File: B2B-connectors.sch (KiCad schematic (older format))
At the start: 2 parts, among them J3 DF40C-100DP-0.4V(51), J4 DF40C-100DP-0.4V(51)

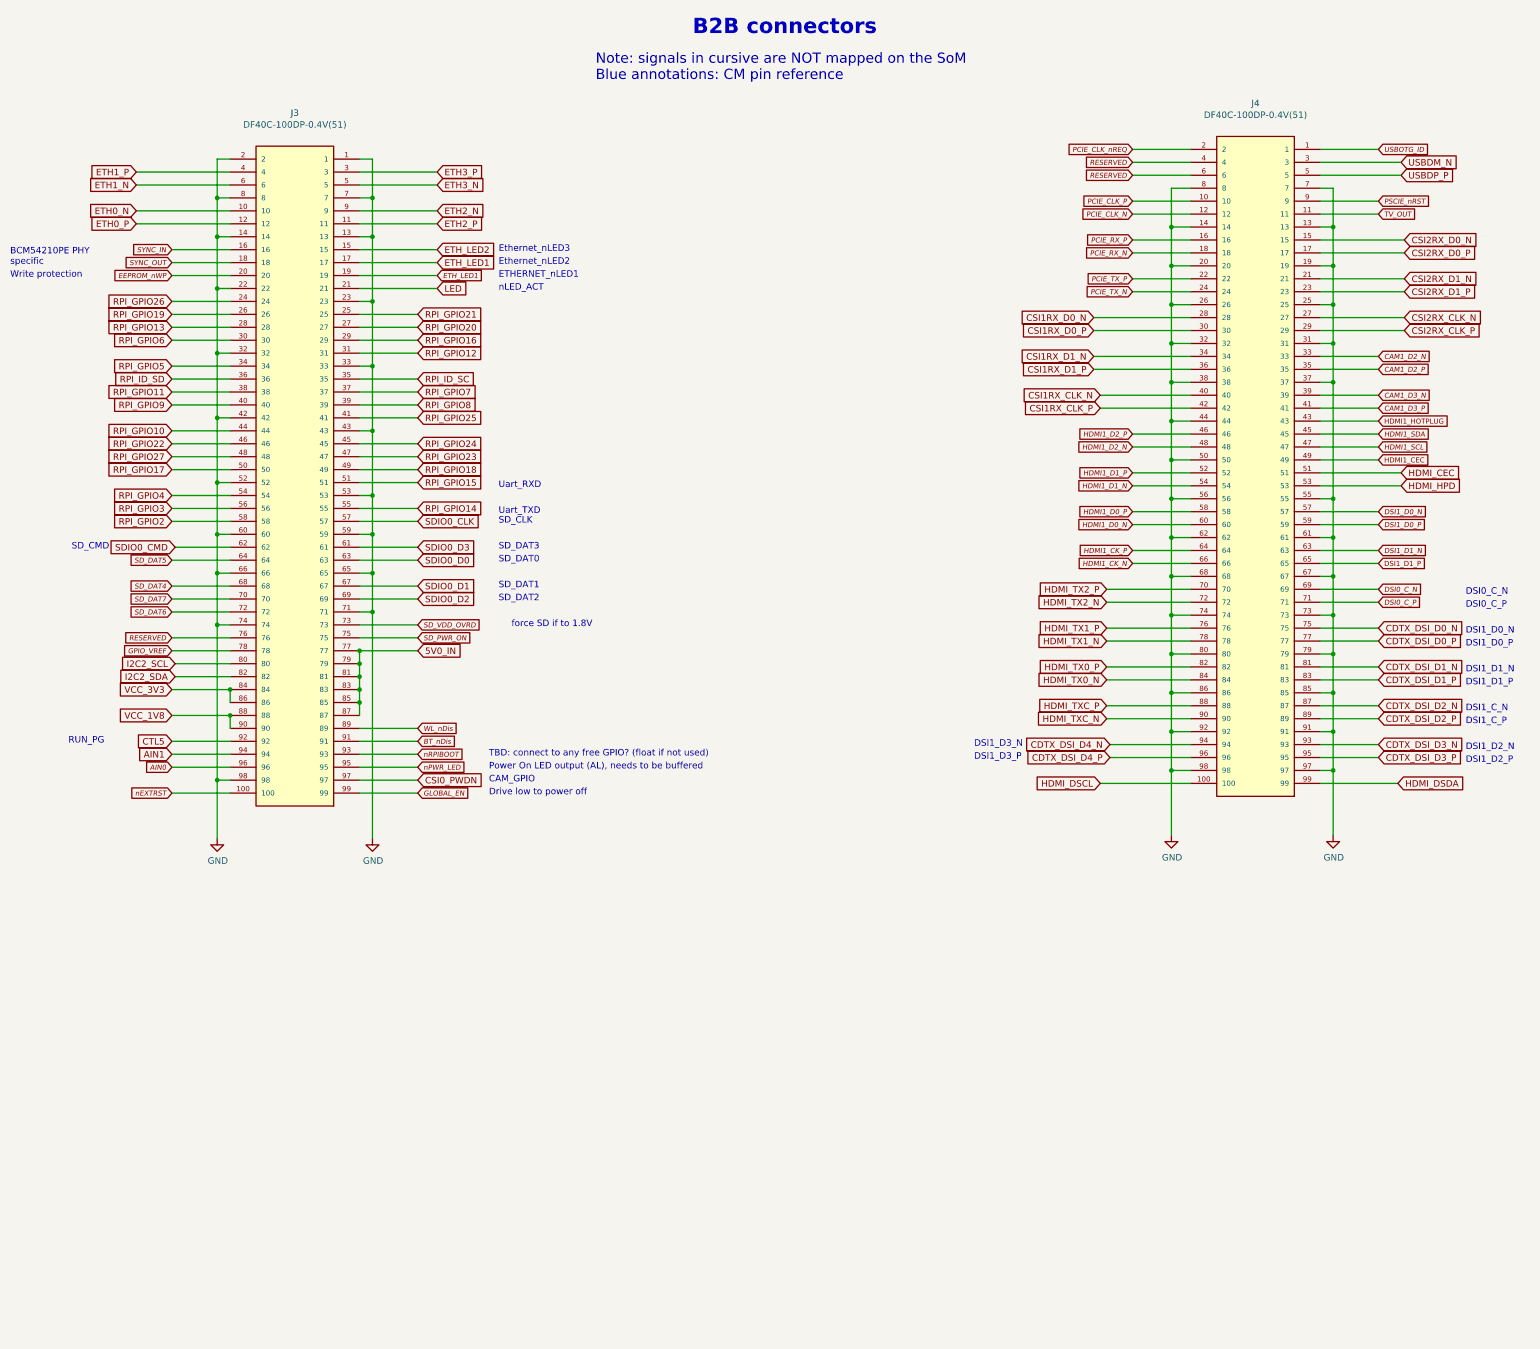
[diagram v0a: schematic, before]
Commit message: Updated GPIO pinout to BV0.9. Remapped DSI. Mapped USB3.0
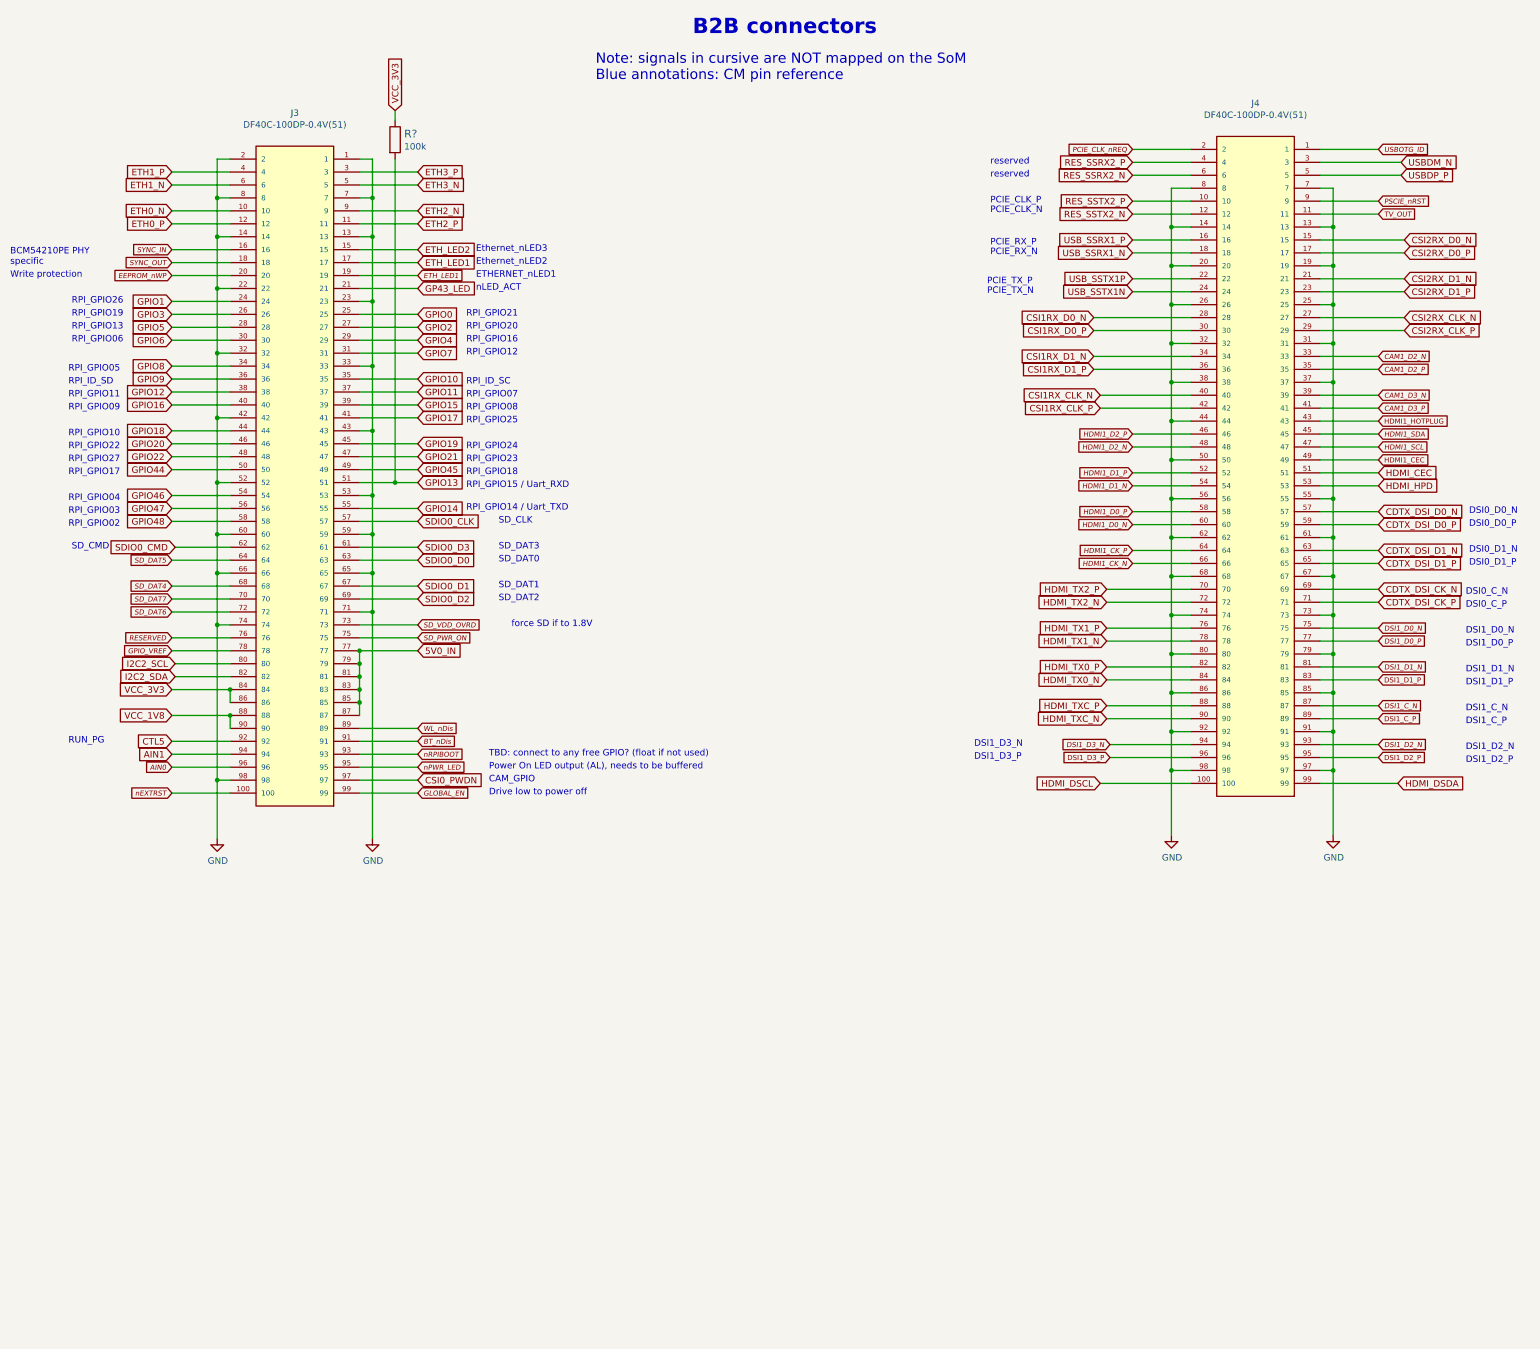
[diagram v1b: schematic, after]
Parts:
- added R?: R_100k_0402, arvsom-footprints:0402-res, symbol arvsom:R_100k_0402
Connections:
- net CDTX_DSI_D0_N: now also J4.57; no longer J4.75
- net CDTX_DSI_D0_P: now also J4.59; no longer J4.77
- net CDTX_DSI_D1_N: now also J4.63; no longer J4.81
- net CDTX_DSI_D1_P: now also J4.65; no longer J4.83
- net DSI1_D0_N: now also J4.75; no longer J4.57
- net DSI1_D0_P: now also J4.77; no longer J4.59
- net DSI1_D1_N: now also J4.81; no longer J4.63
- net DSI1_D1_P: now also J4.83; no longer J4.65
- net RESERVED: no longer J4.4, J4.6
- net VCC_3V3: now also R?.1
- net CDTX_DSI_D2_N renamed DSI1_C_N
- net CDTX_DSI_D2_P renamed DSI1_C_P
- net CDTX_DSI_D3_N renamed DSI1_D2_N
- net CDTX_DSI_D3_P renamed DSI1_D2_P
- net CDTX_DSI_D4_N renamed DSI1_D3_N
- net CDTX_DSI_D4_P renamed DSI1_D3_P
- net DSI0_C_N renamed CDTX_DSI_CK_N
- net DSI0_C_P renamed CDTX_DSI_CK_P
- net LED renamed GP43_LED
- net PCIE_CLK_N renamed RES_SSTX2_N
- net PCIE_CLK_P renamed RES_SSTX2_P
- net PCIE_RX_N renamed USB_SSRX1_N
- net PCIE_RX_P renamed USB_SSRX1_P
- net PCIE_TX_N renamed USB_SSTX1N
- net PCIE_TX_P renamed USB_SSTX1P
- net RPI_GPIO10 renamed GPIO18
- net RPI_GPIO11 renamed GPIO12
- net RPI_GPIO12 renamed GPIO7
- net RPI_GPIO13 renamed GPIO5
- net RPI_GPIO14 renamed GPIO14
- net RPI_GPIO15 renamed GPIO13
- net GPIO13: now also R?.2
- net RPI_GPIO16 renamed GPIO4
- net RPI_GPIO17 renamed GPIO44
- net RPI_GPIO18 renamed GPIO45
- net RPI_GPIO19 renamed GPIO3
- net RPI_GPIO2 renamed GPIO48
- net RPI_GPIO20 renamed GPIO2
- net RPI_GPIO21 renamed GPIO0
- net RPI_GPIO22 renamed GPIO20
- net RPI_GPIO23 renamed GPIO21
- net RPI_GPIO24 renamed GPIO19
- net RPI_GPIO25 renamed GPIO17
- net RPI_GPIO26 renamed GPIO1
- net RPI_GPIO27 renamed GPIO22
- net RPI_GPIO3 renamed GPIO47
- net RPI_GPIO4 renamed GPIO46
- net RPI_GPIO5 renamed GPIO8
- net RPI_GPIO6 renamed GPIO6
- net RPI_GPIO7 renamed GPIO11
- net RPI_GPIO8 renamed GPIO15
- net RPI_GPIO9 renamed GPIO16
- net RPI_ID_SC renamed GPIO10
- net RPI_ID_SD renamed GPIO9
- new net RES_SSRX2_N: J4.6
- new net RES_SSRX2_P: J4.4
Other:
- note added: "DSI0_D0_N"
- note added: "DSI0_D0_P"
- note added: "DSI0_D1_N"
- note added: "DSI0_D1_P"
- note added: "PCIE_CLK_N"
- note added: "PCIE_CLK_P"
- note added: "PCIE_RX_N"
- note added: "PCIE_RX_P"
- note added: "PCIE_TX_N"
- note added: "PCIE_TX_P"
- note added: "RPI_GPIO02"
- note added: "RPI_GPIO03"
- note added: "RPI_GPIO04"
- note added: "RPI_GPIO05"
- note added: "RPI_GPIO06"
- note added: "RPI_GPIO07"
- note added: "RPI_GPIO08"
- note added: "RPI_GPIO09"
- note added: "RPI_GPIO10"
- note added: "RPI_GPIO11"
- note added: "RPI_GPIO12"
- note added: "RPI_GPIO13"
- note added: "RPI_GPIO14 / Uart_TXD"
- note added: "RPI_GPIO15 / Uart_RXD"
- note added: "RPI_GPIO16"
- note added: "RPI_GPIO17"
- note added: "RPI_GPIO18"
- note added: "RPI_GPIO19"
- note added: "RPI_GPIO20"
- note added: "RPI_GPIO21"
- note added: "RPI_GPIO22"
- note added: "RPI_GPIO23"
- note added: "RPI_GPIO24"
- note added: "RPI_GPIO25"
- note added: "RPI_GPIO26"
- note added: "RPI_GPIO27"
- note added: "RPI_ID_SC"
- note added: "RPI_ID_SD"
- note added: "reserved"
- note added: "reserved\n"
- note removed: "Uart_RXD"
- note removed: "Uart_TXD"

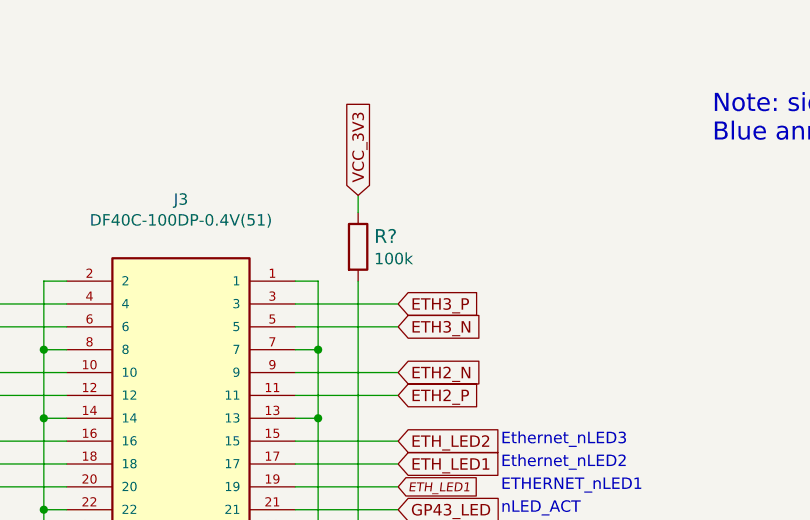
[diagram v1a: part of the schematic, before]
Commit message: Updated VIC config, added reset and crystals
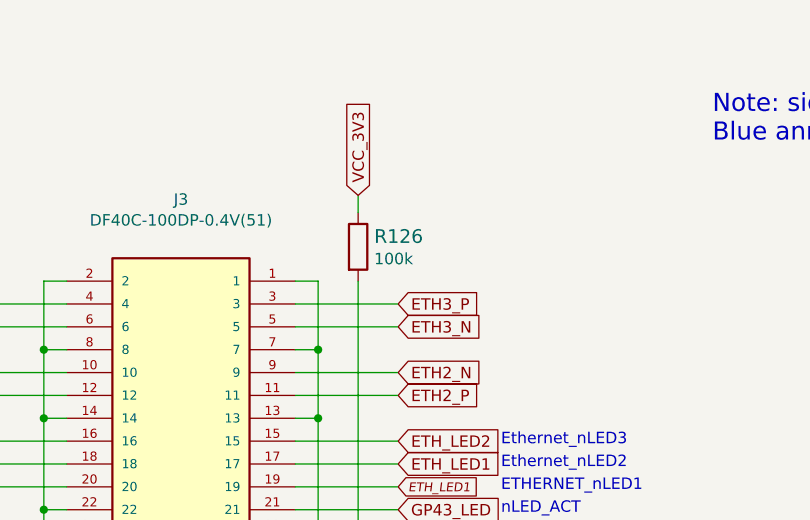
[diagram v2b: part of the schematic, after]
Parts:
- gave numbers to parts that had none: 1
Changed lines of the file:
@@
 	5075 4900 4800 4900
 $Comp
-L arvsom:R_100k_0402 R?
+L arvsom:R_100k_0402 R126
 U 1 1 60AFC161
 P 5075 2250
-F 0 "R?" V 5030 2320 60  0000 L CNN
+F 0 "R126" V 5030 2320 60  0000 L CNN
 F 1 "R_100k_0402" H 5075 2100 60  0001 C CNN
 F 2 "arvsom-footprints:0402-res" H 5275 2450 60  0001 L CNN

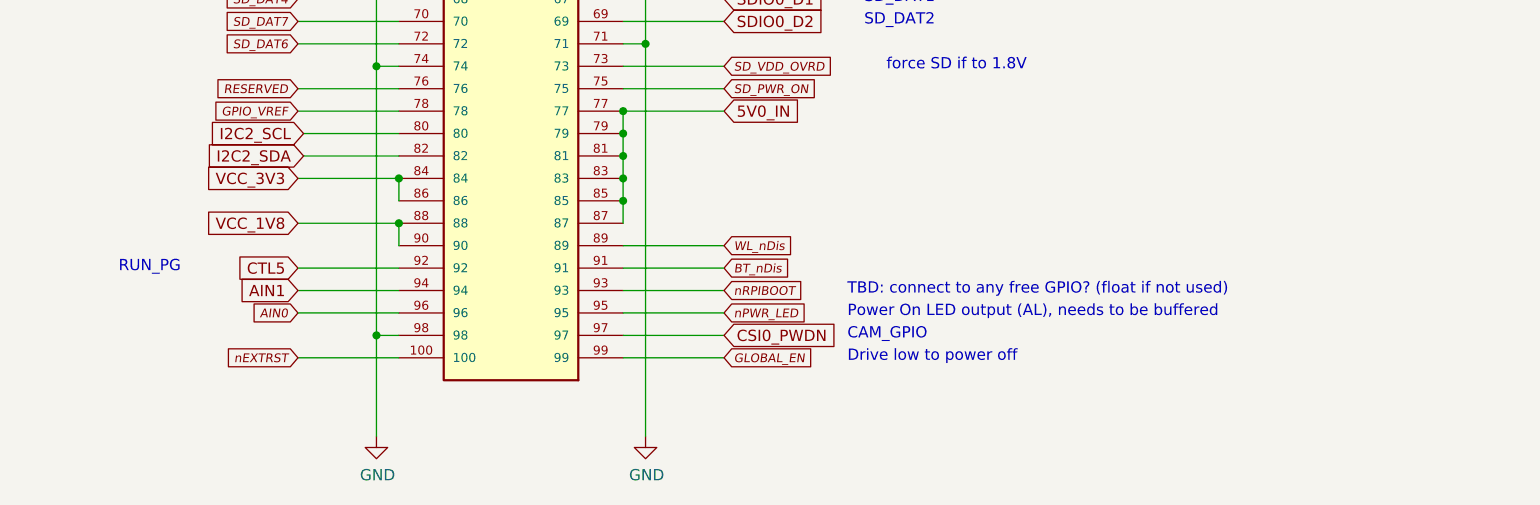
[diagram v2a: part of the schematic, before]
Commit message: Added BOOT_FROM_UART and power LED. Changed LED transistor to smaller footprint
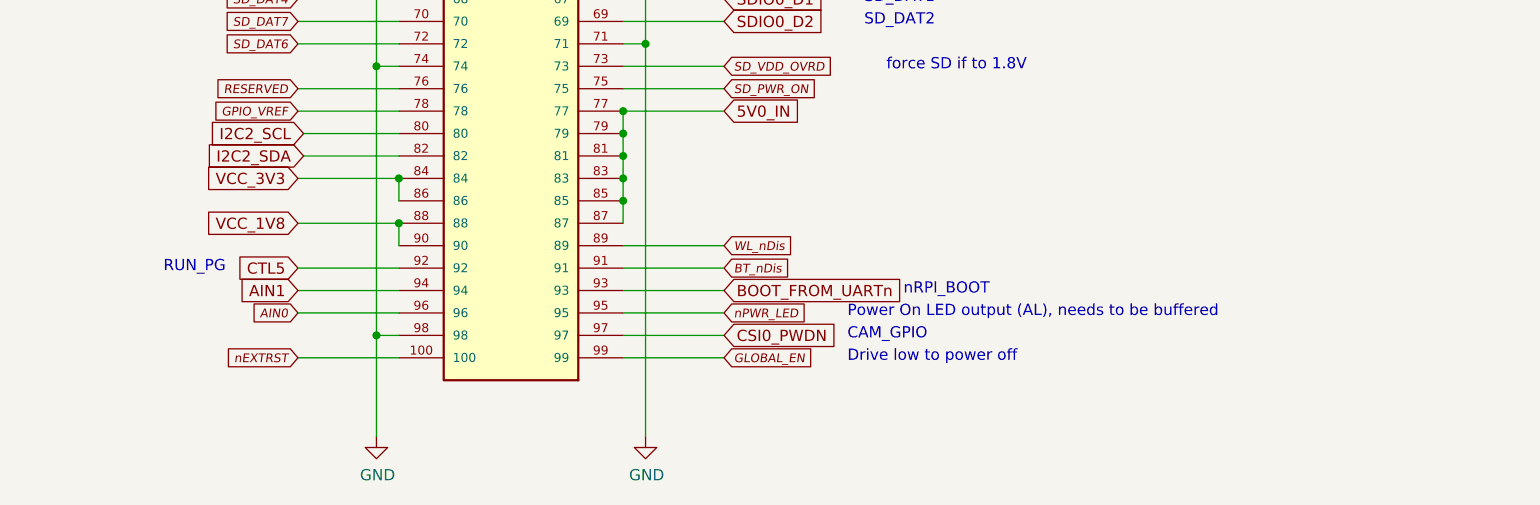
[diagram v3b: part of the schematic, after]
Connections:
- net nRPIBOOT renamed BOOT_FROM_UARTn
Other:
- note added: "nRPI_BOOT"
- note removed: "TBD: connect to any free GPIO? (float if not used)"
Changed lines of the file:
@@
 Wire Wire Line
 	4800 7000 5250 7000
-Text GLabel 5250 7000 2    39   Input Italic 0
-nRPIBOOT
 Wire Wire Line
 	11225 2425 10775 2425
@@
 Text Notes 5800 7225 0    50   ~ 0
 CAM_GPIO
-Text Notes 5800 7025 0    50   ~ 0
-TBD: connect to any free GPIO? (float if not used)
+Text Notes 6050 7025 0    50   ~ 0
+nRPI_BOOT
 Text Notes 5800 7125 0    50   ~ 0
 Power On LED output (AL), needs to be buffered
 Text Notes 5800 7325 0    50   ~ 0
 Drive low to power off
-Text Notes 2550 6925 0    50   ~ 0
+Text Notes 2750 6925 0    50   ~ 0
 RUN_PG
 Text Notes 13350 5775 0    50   ~ 0
@@
 Text Notes 9650 3450 0    50   ~ 0
 PCIE_TX_N
+Text GLabel 5250 7000 2    50   Input ~ 0
+BOOT_FROM_UARTn
 $EndSCHEMATC

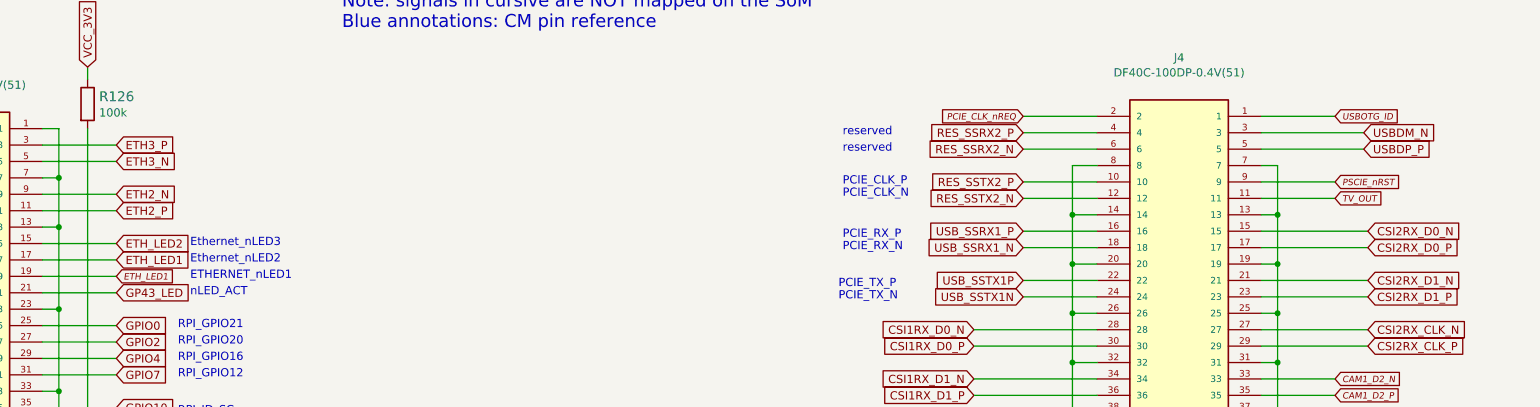
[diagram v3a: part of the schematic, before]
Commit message: Routed USB, QSPI, JTAG
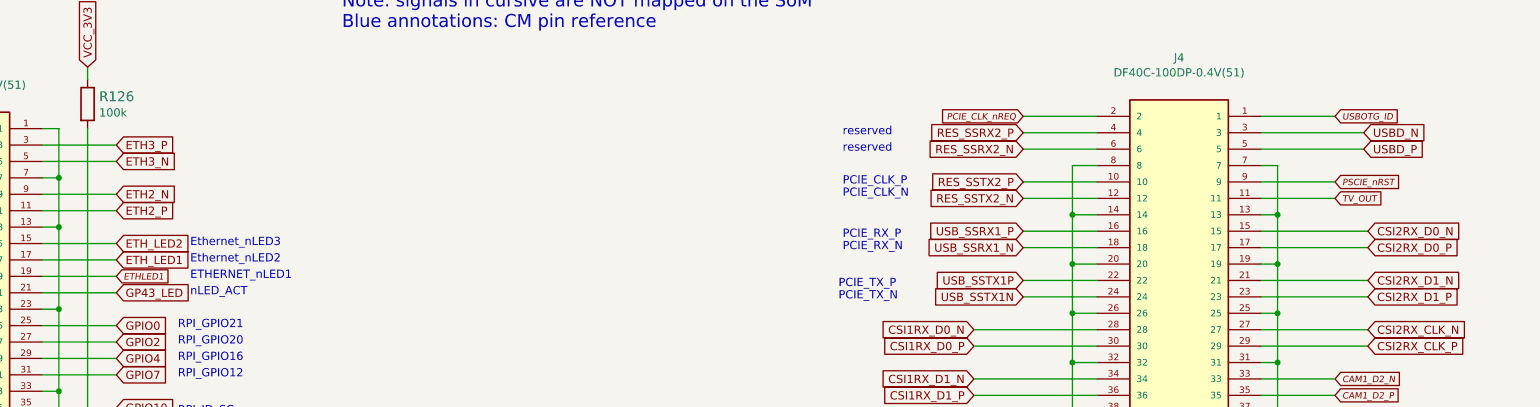
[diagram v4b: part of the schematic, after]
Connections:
- net ETH_LED1: no longer J3.19
- net USBDM_N renamed USBD_N
- net USBDP_P renamed USBD_P
- new net ETHLED1: J3.19
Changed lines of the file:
@@
 Connection ~ 4800 6200
 Text GLabel 12850 2425 2    50   Input ~ 0
-USBDM_N
+USBD_N
 Text GLabel 12850 2525 2    50   Input ~ 0
-USBDP_P
+USBD_P
 Text GLabel 12875 3025 2    50   Input ~ 0
 CSI2RX_D0_N
@@
 B2B connectors
 Text GLabel 5250 3300 2    39   Input Italic 0
-ETH_LED1
+ETHLED1
 Wire Wire Line
 	4800 3300 5250 3300
